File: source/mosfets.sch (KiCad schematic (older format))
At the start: 78 parts, among them Q1 NCEP60T20, Q10 Q_PNP_BCE, Q11 Q_PNP_BCE, Q12 Q_PNP_BCE, Q2 NCEP60T20, Q3 NCEP60T20, Q4 NCEP60T20, Q5 NCEP60T20, Q6 NCEP60T20, Q7 Q_PNP_BCE, Q8 Q_PNP_BCE, Q9 Q_PNP_BCE

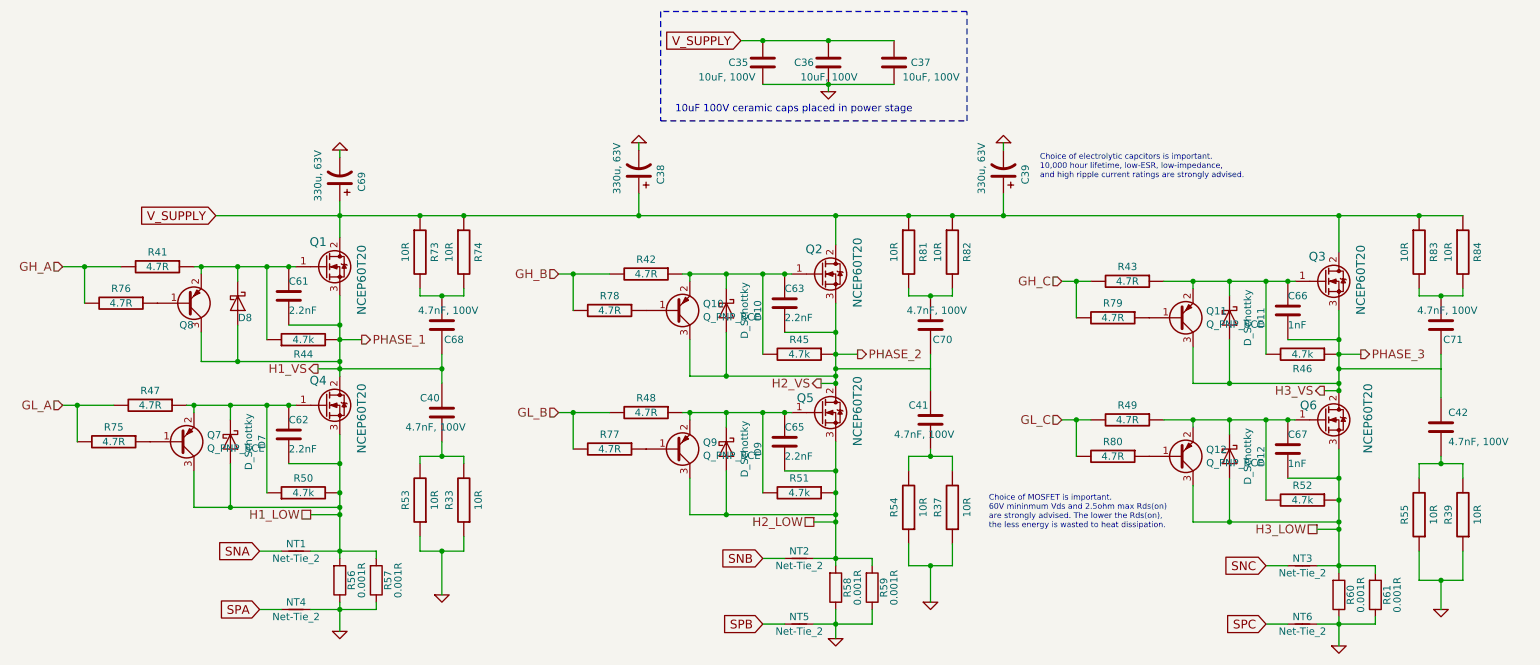
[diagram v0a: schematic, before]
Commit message: Removed gate transistors
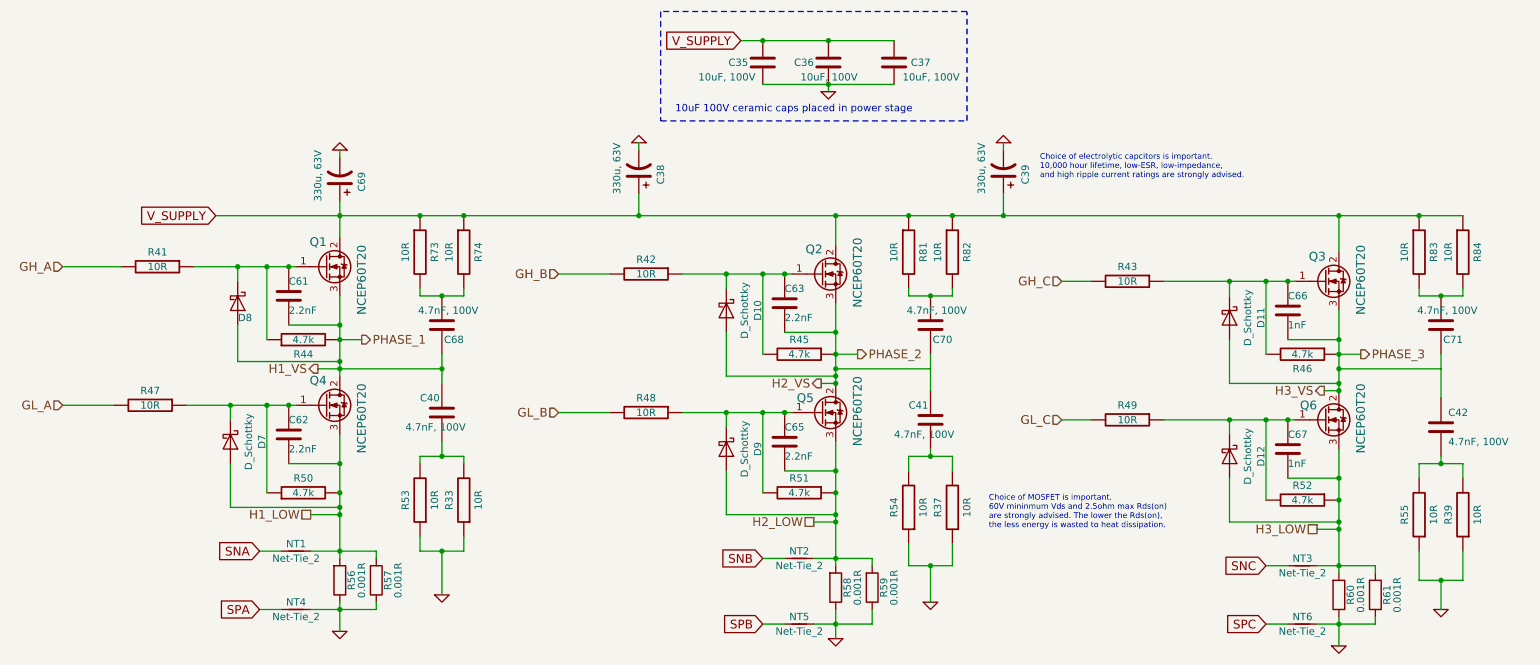
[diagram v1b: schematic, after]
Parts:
- removed Q10, Q11, Q12, Q7, Q8, Q9: Q_PNP_BCE, Package_TO_SOT_SMD:SOT-23, symbol Device:Q_PNP_BEC
- removed R75, R76, R77, R78, R79, R80: 4.7R, Resistor_SMD:R_0603_1608Metric, symbol BLDC_4-rescue:R-RESCUE-BLDC_4
- R41, R42, R43, R47, R48, R49: value 4.7R -> 10R
